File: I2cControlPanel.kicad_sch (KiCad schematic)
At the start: 46 parts

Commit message: Assign asukiaaa-kicad- symbols and footprints
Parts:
- D4, D5, D6: symbol my-kicad-symbols:Diode_4array_1SS309 -> asukiaaa-kicad-symbols:Diode_4array_1SS309
- U1: symbol my-kicad-symbols:NJM12888F33 -> asukiaaa-kicad-symbols:NJM12888F33
- U3: symbol my-kicad-symbols:AQM0802 -> asukiaaa-kicad-symbols:AQM0802

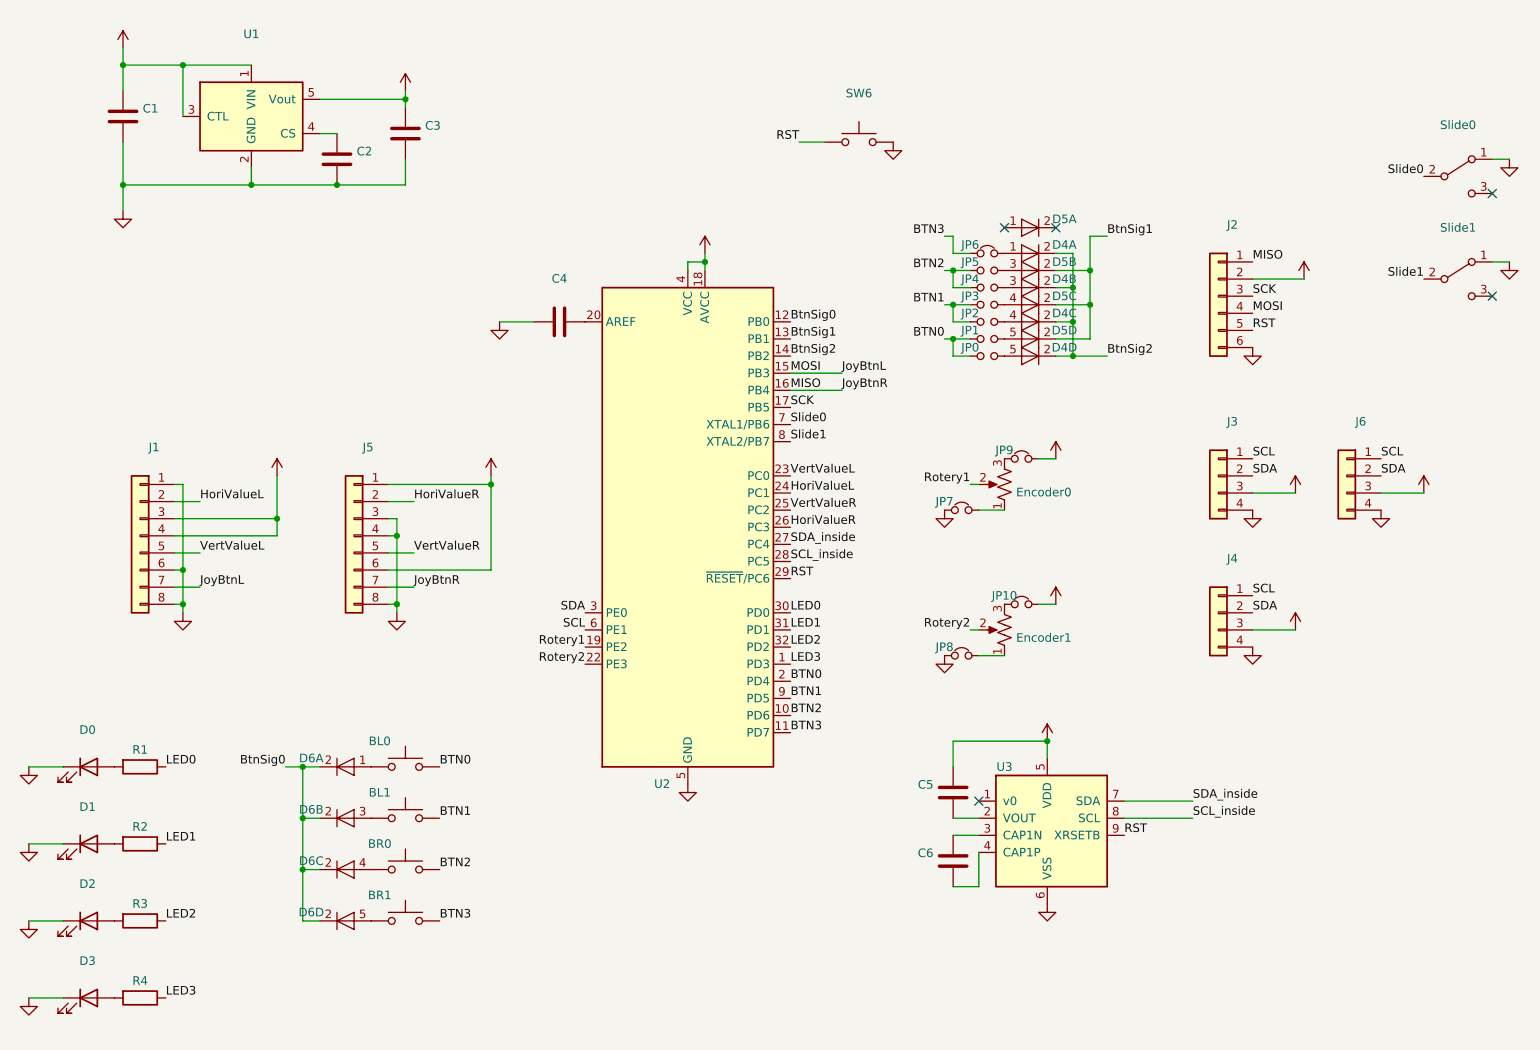
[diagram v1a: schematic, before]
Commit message: Add A package for ATmega328PB
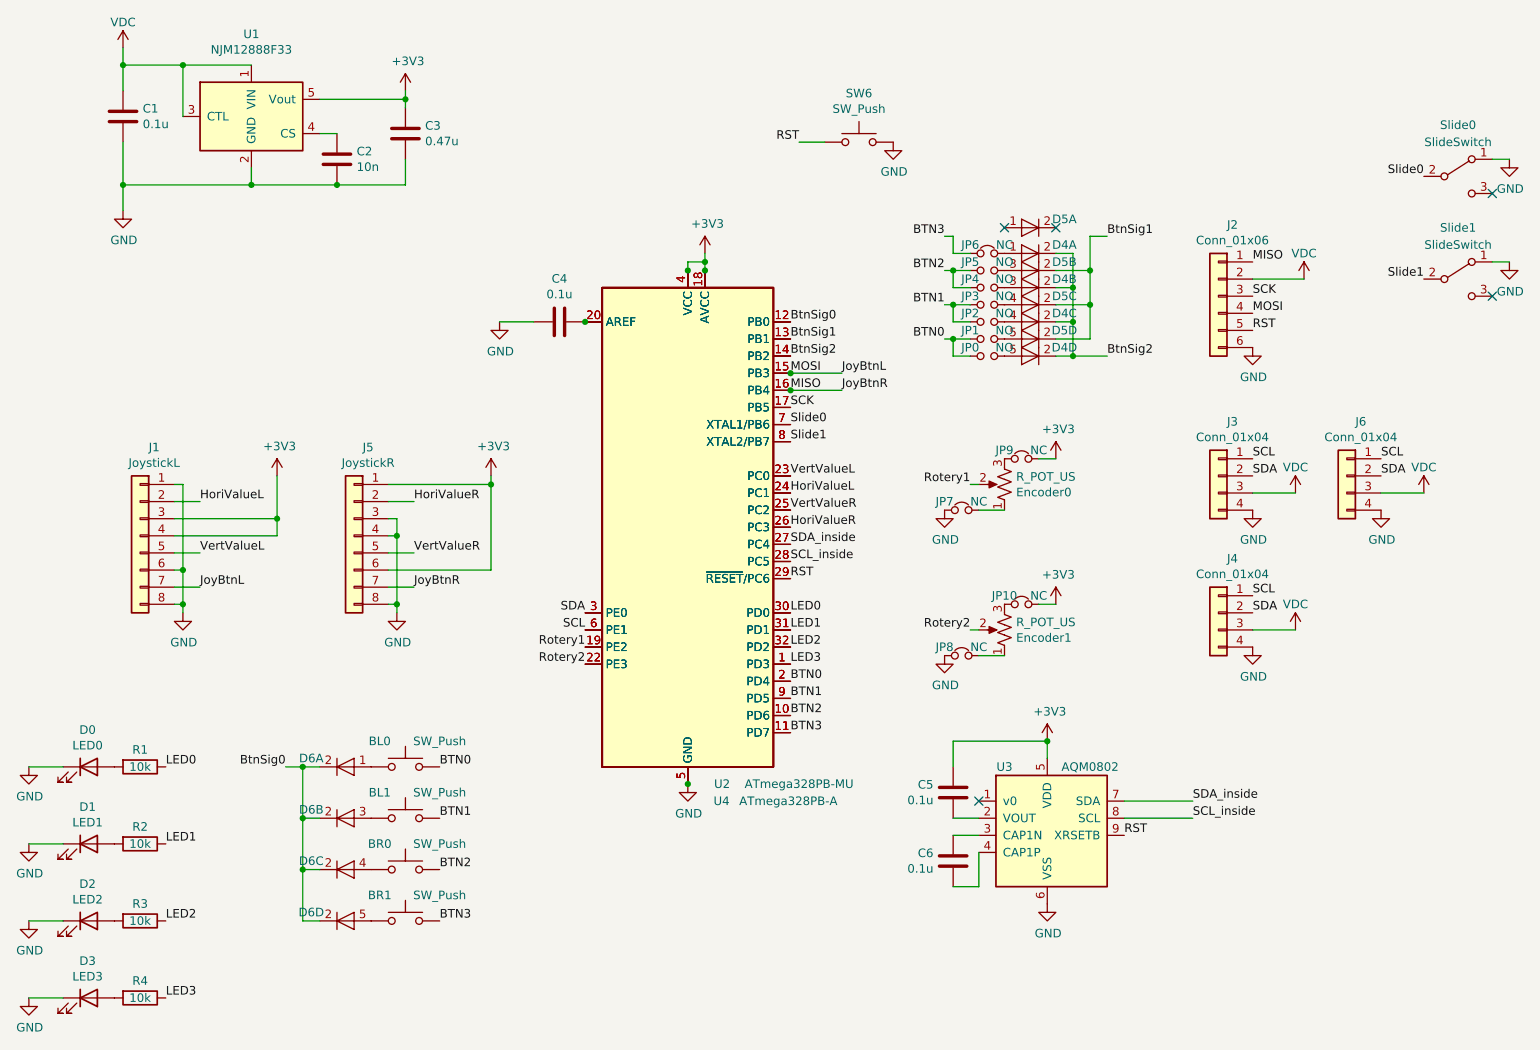
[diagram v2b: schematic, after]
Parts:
- added U4: ATmega328PB-A, asukiaaa-kicad-footprints:TQFP-32_7x7mm_P0.8mm_short_inner, symbol MCU_Microchip_ATmega:ATmega328PB-A
- BL0, BL1, BR0, BR1: value (none) -> SW_Push; footprint (none) -> footprints:SW_Center_PUSH-12mm
- C1, C4, C5, C6: value (none) -> 0.1u; footprint (none) -> Capacitor_SMD:C_0402_1005Metric
- C2: value (none) -> 10n; footprint (none) -> Capacitor_SMD:C_0603_1608Metric
- C3: value (none) -> 0.47u; footprint (none) -> Capacitor_SMD:C_0402_1005Metric
- D0: value (none) -> LED0; footprint (none) -> Diode_SMD:D_0603_1608Metric_Pad1.05x0.95mm_HandSolder
- D1: value (none) -> LED1; footprint (none) -> Diode_SMD:D_0603_1608Metric_Pad1.05x0.95mm_HandSolder
- D2: value (none) -> LED2; footprint (none) -> Diode_SMD:D_0603_1608Metric_Pad1.05x0.95mm_HandSolder
- D3: value (none) -> LED3; footprint (none) -> Diode_SMD:D_0603_1608Metric_Pad1.05x0.95mm_HandSolder
- D4, D5, D6: value (none) -> 1SS309; footprint (none) -> asukiaaa-kicad-footprints:SC-74-5_1.6x2.9mm_P0.95mm
- Encoder0, Encoder1: value (none) -> R_POT_US; footprint (none) -> asukiaaa-kicad-footprints:RoteryEncoderWithPowerLabel
- J1: value (none) -> JoystickL; footprint (none) -> asukiaaa-kicad-footprints:PS4tJoystick
- J2: value (none) -> Conn_01x06; footprint (none) -> asukiaaa-kicad-footprints:2x03_P2.54mm_Pads
- J3, J6: value (none) -> Conn_01x04; footprint (none) -> footprints:NS-Tech_Grove_1x04_P2mm_Horizontal
- J4: value (none) -> Conn_01x04; footprint (none) -> TerminalBlock:TerminalBlock_bornier-4_P5.08mm
- J5: value (none) -> JoystickR; footprint (none) -> asukiaaa-kicad-footprints:PS4tJoystick
- JP0, JP1, JP2, JP3, JP4, JP5: value (none) -> NO; footprint (none) -> Jumper:SolderJumper-2_P1.3mm_Open_RoundedPad1.0x1.5mm
- JP10, JP6, JP7, JP8, JP9: value (none) -> NC; footprint (none) -> Jumper:SolderJumper-2_P1.3mm_Bridged_RoundedPad1.0x1.5mm
- R1, R2, R3, R4: value (none) -> 10k; footprint (none) -> Resistor_SMD:R_0603_1608Metric
- SW6: value (none) -> SW_Push; footprint (none) -> Button_Switch_THT:SW_PUSH_6mm
- Slide0, Slide1: value (none) -> SlideSwitch; footprint (none) -> asukiaaa-kicad-footprints:SlideSwitch_SS12D01G4_2posi_1line
- U1: value (none) -> NJM12888F33; footprint (none) -> Package_TO_SOT_SMD:SOT-23-5
- U2: value (none) -> ATmega328PB-MU; footprint (none) -> Package_DFN_QFN:QFN-32-1EP_5x5mm_P0.5mm_EP3.1x3.1mm
- U3: value (none) -> AQM0802; footprint (none) -> asukiaaa-kicad-footprints:AQM0802A-RN-GBW
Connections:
- net +3V3: now also U4.18 (AVCC), U4.4 (VCC)
- net BTN0: now also U4.2 (PD4)
- net BTN1: now also U4.9 (PD5)
- net BTN2: now also U4.10 (PD6)
- net BTN3: now also U4.11 (PD7)
- net BtnSig0: now also U4.12 (PB0)
- net BtnSig1: now also U4.13 (PB1)
- net BtnSig2: now also U4.14 (PB2)
- net GND: now also U4.21 (GND), U4.5 (GND)
- net HoriValueL: now also U4.24 (PC1)
- net HoriValueR: now also U4.26 (PC3)
- net JoyBtnL: now also U4.15 (PB3)
- net JoyBtnR: now also U4.16 (PB4)
- net LED0: now also U4.30 (PD0)
- net LED1: now also U4.31 (PD1)
- net LED2: now also U4.32 (PD2)
- net LED3: now also U4.1 (PD3)
- net RST: now also U4.29 (~{RESET}/PC6)
- net Rotery1: now also U4.19 (PE2)
- net Rotery2: now also U4.22 (PE3)
- net SCK: now also U4.17 (PB5)
- net SCL: now also U4.6 (PE1)
- net SCL_inside: now also U4.28 (PC5)
- net SDA: now also U4.3 (PE0)
- net SDA_inside: now also U4.27 (PC4)
- net Slide0: now also U4.7 (XTAL1/PB6)
- net Slide1: now also U4.8 (XTAL2/PB7)
- net VertValueL: now also U4.23 (PC0)
- net VertValueR: now also U4.25 (PC2)
- net at C4.2, U2.20 (AREF): now also U4.20 (AREF)
